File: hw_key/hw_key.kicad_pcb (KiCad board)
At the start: 2 copper layers, 127 x 38.1 mm, 27 parts, among them P2 CONN_01X10, SW1 SW_PUSH_SMALL_H, SW10 SW_PUSH_SMALL_H, SW11 SW_PUSH_SMALL_H, SW12 SW_PUSH_SMALL_H, SW2 SW_PUSH_SMALL_H, SW3 SW_PUSH_SMALL_H, SW4 SW_PUSH_SMALL_H, SW5 SW_PUSH_SMALL_H, SW6 SW_PUSH_SMALL_H, SW7 SW_PUSH_SMALL_H, SW8 SW_PUSH_SMALL_H, SW9 SW_PUSH_SMALL_H

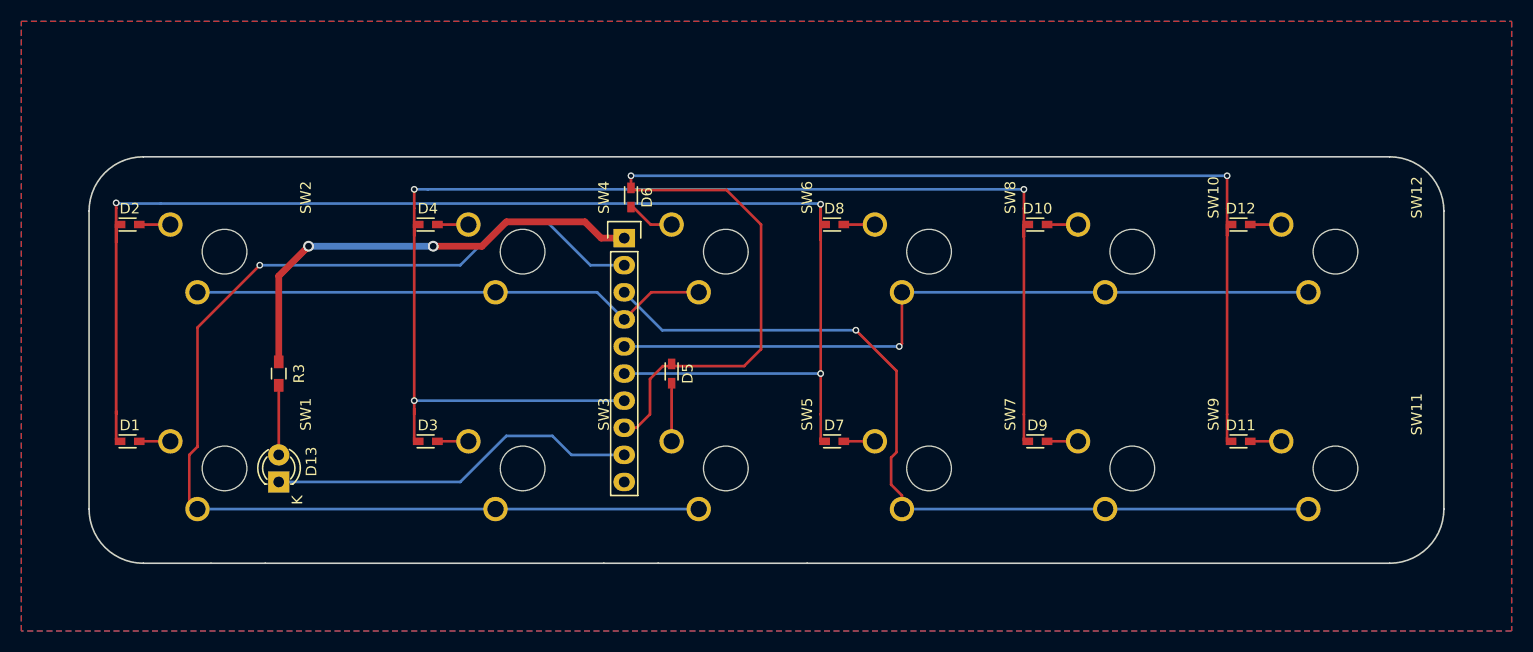
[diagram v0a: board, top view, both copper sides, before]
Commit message: misc, rst button 3d model
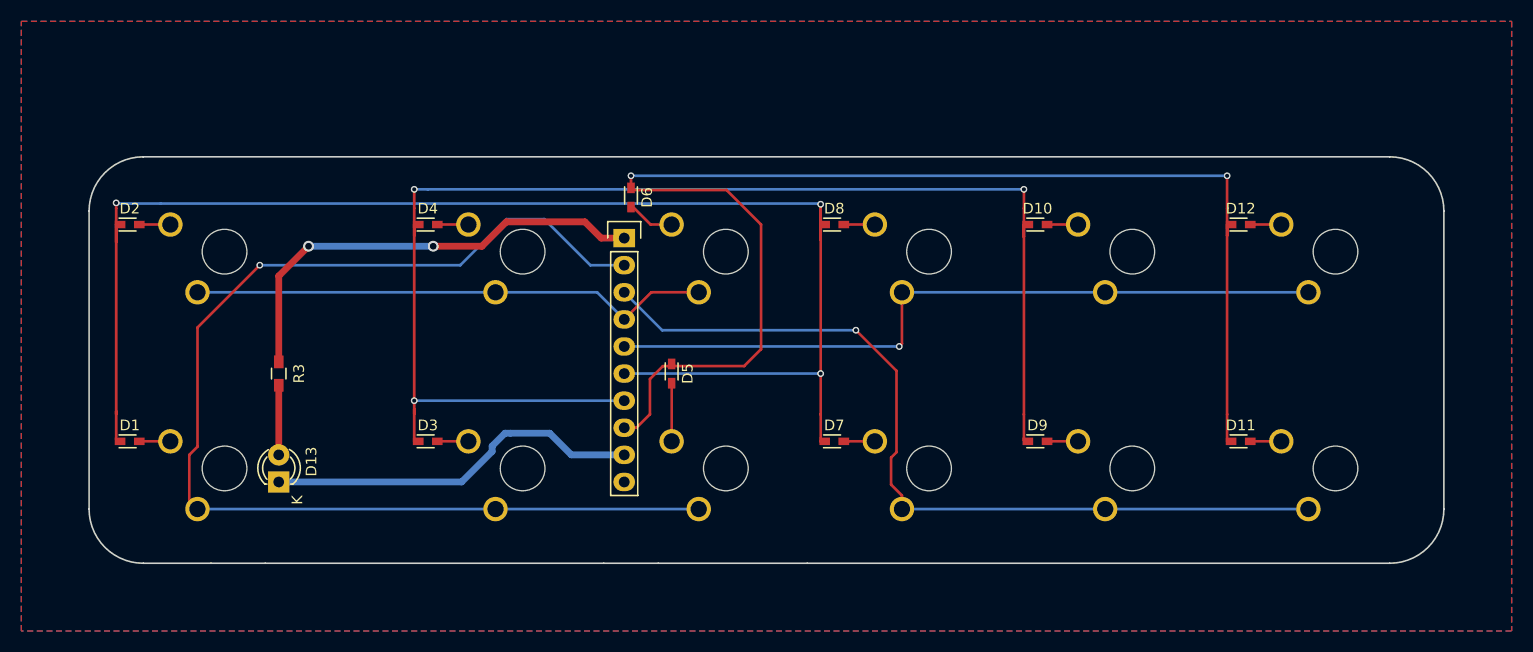
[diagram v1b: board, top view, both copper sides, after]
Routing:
- net /kLED_MACRO: track 34.9 -> 35.4 mm
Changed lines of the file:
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@@
     (thickness 1.6)
     (drawings 14)
-    (tracks 137)
+    (tracks 140)
     (zones 0)
     (modules 27)
@@
     (visible_elements 7FFEFFFF)
     (pcbplotparams
-      (layerselection 0x00030_80000001)
-      (usegerberextensions false)
+      (layerselection 0x010fc_80000001)
+      (usegerberextensions true)
       (excludeedgelayer true)
       (linewidth 0.100000)
       (plotframeref false)
-      (viasonmask false)
+      (viasonmask true)
       (mode 1)
-      (useauxorigin false)
+      (useauxorigin true)
       (hpglpennumber 1)
       (hpglpenspeed 20)
@@
       (psa4output false)
       (plotreference true)
-      (plotvalue true)
+      (plotvalue false)
       (plotinvisibletext false)
       (padsonsilk false)
-      (subtractmaskfromsilk false)
+      (subtractmaskfromsilk true)
       (outputformat 1)
       (mirror false)
-      (drillshape 1)
+      (drillshape 0)
       (scaleselection 1)
-      (outputdirectory ""))
+      (outputdirectory grb))
   )
   (net 0 "")
@@
     (add_net /kC2)
     (add_net /kC3)
-    (add_net /kLED_MACRO)
     (add_net /kR0)
     (add_net /kR1)
@@
     (add_net "Net-(D11-Pad2)")
     (add_net "Net-(D12-Pad2)")
-    (add_net "Net-(D13-Pad2)")
     (add_net "Net-(D2-Pad2)")
     (add_net "Net-(D3-Pad2)")
@@
     (uvia_drill 0.1016)
     (add_net +3V3)
+    (add_net /kLED_MACRO)
     (add_net GND)
+    (add_net "Net-(D13-Pad2)")
   )
   (module Pin_Headers:Pin_Header_Straight_1x10 (layer F.Cu)
@@
   (module components:CHERRY_MX (layer F.Cu)
     (at 38.1 54.61 90)
-    (fp_text reference SW1 (at 5.08 7.62 90) (layer F.SilkS)
+    (fp_text reference SW1 (at 5.08 7.62 90) (layer F.SilkS) hide
       (effects (font (size 1 1) (thickness 0.15)))
     )
@@
   (module components:CHERRY_MX (layer F.Cu)
     (at 38.1 34.29 90)
-    (fp_text reference SW2 (at 5.08 7.62 90) (layer F.SilkS)
+    (fp_text reference SW2 (at 5.08 7.62 90) (layer F.SilkS) hide
       (effects (font (size 1 1) (thickness 0.15)))
     )
@@
   (module components:CHERRY_MX (layer F.Cu)
     (at 66.04 54.61 90)
-    (fp_text reference SW3 (at 5.08 7.62 90) (layer F.SilkS)
+    (fp_text reference SW3 (at 5.08 7.62 90) (layer F.SilkS) hide
       (effects (font (size 1 1) (thickness 0.15)))
     )
@@
   (module components:CHERRY_MX (layer F.Cu)
     (at 66.04 34.29 90)
-    (fp_text reference SW4 (at 5.08 7.62 90) (layer F.SilkS)
+    (fp_text reference SW4 (at 5.08 7.62 90) (layer F.SilkS) hide
       (effects (font (size 1 1) (thickness 0.15)))
     )
@@
   (module components:CHERRY_MX (layer F.Cu)
     (at 85.09 54.61 90)
-    (fp_text reference SW5 (at 5.08 7.62 90) (layer F.SilkS)
+    (fp_text reference SW5 (at 5.08 7.62 90) (layer F.SilkS) hide
       (effects (font (size 1 1) (thickness 0.15)))
     )
@@
   (module components:CHERRY_MX (layer F.Cu)
     (at 85.09 34.29 90)
-    (fp_text reference SW6 (at 5.08 7.62 90) (layer F.SilkS)
+    (fp_text reference SW6 (at 5.08 7.62 90) (layer F.SilkS) hide
       (effects (font (size 1 1) (thickness 0.15)))
     )
@@
   (module components:CHERRY_MX (layer F.Cu)
     (at 104.14 54.61 90)
-    (fp_text reference SW7 (at 5.08 7.62 90) (layer F.SilkS)
+    (fp_text reference SW7 (at 5.08 7.62 90) (layer F.SilkS) hide
       (effects (font (size 1 1) (thickness 0.15)))
     )
@@
   (module components:CHERRY_MX (layer F.Cu)
     (at 104.14 34.29 90)
-    (fp_text reference SW8 (at 5.08 7.62 90) (layer F.SilkS)
+    (fp_text reference SW8 (at 5.08 7.62 90) (layer F.SilkS) hide
       (effects (font (size 1 1) (thickness 0.15)))
     )
@@
   (module components:CHERRY_MX (layer F.Cu)
     (at 123.19 54.61 90)
-    (fp_text reference SW9 (at 5.08 7.62 90) (layer F.SilkS)
+    (fp_text reference SW9 (at 5.08 7.62 90) (layer F.SilkS) hide
       (effects (font (size 1 1) (thickness 0.15)))
     )
@@
   (module components:CHERRY_MX (layer F.Cu)
     (at 123.19 34.29 90)
-    (fp_text reference SW10 (at 5.08 7.62 90) (layer F.SilkS)
+    (fp_text reference SW10 (at 5.08 7.62 90) (layer F.SilkS) hide
       (effects (font (size 1 1) (thickness 0.15)))
     )
@@
   (module components:CHERRY_MX (layer F.Cu)
     (at 142.24 54.61 90)
-    (fp_text reference SW11 (at 5.08 7.62 90) (layer F.SilkS)
+    (fp_text reference SW11 (at 5.08 7.62 90) (layer F.SilkS) hide
       (effects (font (size 1 1) (thickness 0.15)))
     )
@@
   (module components:CHERRY_MX (layer F.Cu)
     (at 142.24 34.29 90)
-    (fp_text reference SW12 (at 5.08 7.62 90) (layer F.SilkS)
+    (fp_text reference SW12 (at 5.08 7.62 90) (layer F.SilkS) hide
       (effects (font (size 1 1) (thickness 0.15)))
     )
@@
   (segment (start 137.16 52.07) (end 134.25 52.07) (width 0.254) (layer F.Cu) (net 11))
   (segment (start 137.16 31.75) (end 134.25 31.75) (width 0.254) (layer F.Cu) (net 12))
-  (segment (start 43.18 53.34) (end 43.18 46.82) (width 0.254) (layer F.Cu) (net 13) (status 30))
+  (segment (start 43.18 53.34) (end 43.18 46.82) (width 0.635) (layer F.Cu) (net 13) (status 30))
   (segment (start 43.18 44.62) (end 43.18 36.576) (width 0.635) (layer F.Cu) (net 14) (status 10))
   (segment (start 73.406 33.02) (end 75.565 33.02) (width 0.635) (layer F.Cu) (net 14) (status 20))
@@
   (segment (start 88.392 43.434) (end 88.392 31.75) (width 0.254) (layer F.Cu) (net 17))
   (segment (start 86.806 45.02) (end 88.392 43.434) (width 0.254) (layer F.Cu) (net 17))
-  (segment (start 75.565 53.34) (end 70.612 53.34) (width 0.254) (layer B.Cu) (net 18))
-  (segment (start 60.198 55.88) (end 43.18 55.88) (width 0.254) (layer B.Cu) (net 18))
-  (segment (start 64.516 51.562) (end 60.198 55.88) (width 0.254) (layer B.Cu) (net 18))
-  (segment (start 68.834 51.562) (end 64.516 51.562) (width 0.254) (layer B.Cu) (net 18))
-  (segment (start 70.612 53.34) (end 68.834 51.562) (width 0.254) (layer B.Cu) (net 18))
+  (segment (start 64.897 51.308) (end 64.389 51.308) (width 0.635) (layer B.Cu) (net 18))
+  (segment (start 70.612 53.34) (end 68.58 51.308) (width 0.635) (layer B.Cu) (net 18))
+  (segment (start 68.58 51.308) (end 64.897 51.308) (width 0.635) (layer B.Cu) (net 18))
+  (segment (start 43.18 55.88) (end 60.325 55.88) (width 0.635) (layer B.Cu) (net 18) (status 400000))
+  (segment (start 70.612 53.34) (end 75.565 53.34) (width 0.635) (layer B.Cu) (net 18))
+  (segment (start 63.1825 53.0225) (end 60.325 55.88) (width 0.635) (layer B.Cu) (net 18))
+  (segment (start 63.1825 52.5145) (end 63.1825 53.0225) (width 0.635) (layer B.Cu) (net 18))
+  (segment (start 64.389 51.308) (end 63.1825 52.5145) (width 0.635) (layer B.Cu) (net 18))
   (segment (start 75.565 43.18) (end 101.346 43.18) (width 0.254) (layer B.Cu) (net 19) (status 10))
   (segment (start 101.6 42.926) (end 101.6 38.1) (width 0.254) (layer F.Cu) (net 19) (status 20))
@@
   (segment (start 34.798 57.658) (end 34.798 53.34) (width 0.254) (layer F.Cu) (net 21) (status 10))
   (segment (start 72.39 35.56) (end 75.565 35.56) (width 0.254) (layer B.Cu) (net 21) (status 20))
-  (segment (start 68.326 31.496) (end 72.39 35.56) (width 0.254) (layer B.Cu) (net 21))
-  (segment (start 64.262 31.496) (end 68.326 31.496) (width 0.254) (layer B.Cu) (net 21))
-  (segment (start 60.198 35.56) (end 64.262 31.496) (width 0.254) (layer B.Cu) (net 21))
+  (segment (start 68.072 31.242) (end 72.39 35.56) (width 0.254) (layer B.Cu) (net 21))
+  (segment (start 64.516 31.242) (end 68.072 31.242) (width 0.254) (layer B.Cu) (net 21))
+  (segment (start 60.198 35.56) (end 64.516 31.242) (width 0.254) (layer B.Cu) (net 21))
   (segment (start 41.402 35.56) (end 60.198 35.56) (width 0.254) (layer B.Cu) (net 21))
   (via (at 41.402 35.56) (size 0.635) (drill 0.381) (layers F.Cu B.Cu) (net 21))

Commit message: mounting holes
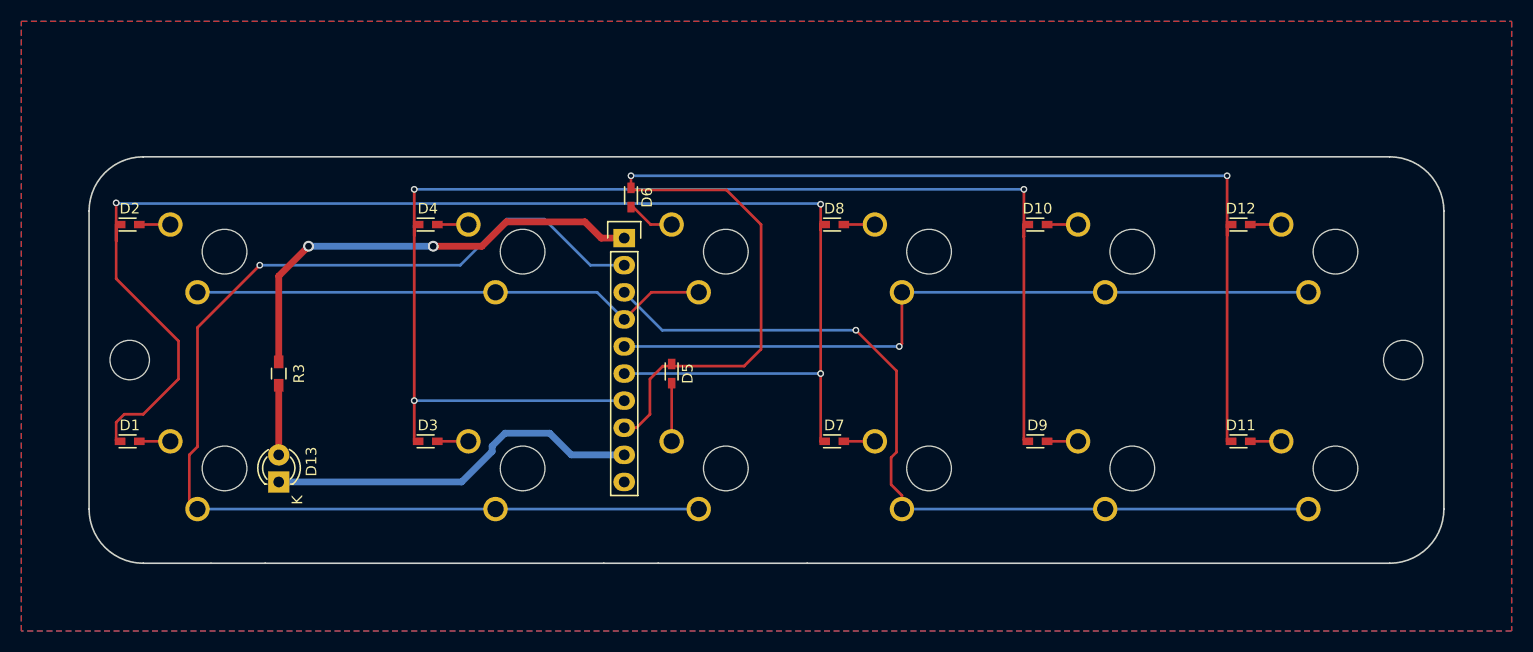
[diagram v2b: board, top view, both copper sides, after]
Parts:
- added REF**: MountingHole_3.7mm, Mounting_Holes:MountingHole_3.7mm, F.Cu at (148.6, 44.5)
- added REF**: MountingHole_3.7mm, Mounting_Holes:MountingHole_3.7mm, F.Cu at (29.2, 44.5)
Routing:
- net /kR0: track 136.0 -> 139.1 mm
- net /kR1: track 128.2 -> 127.6 mm

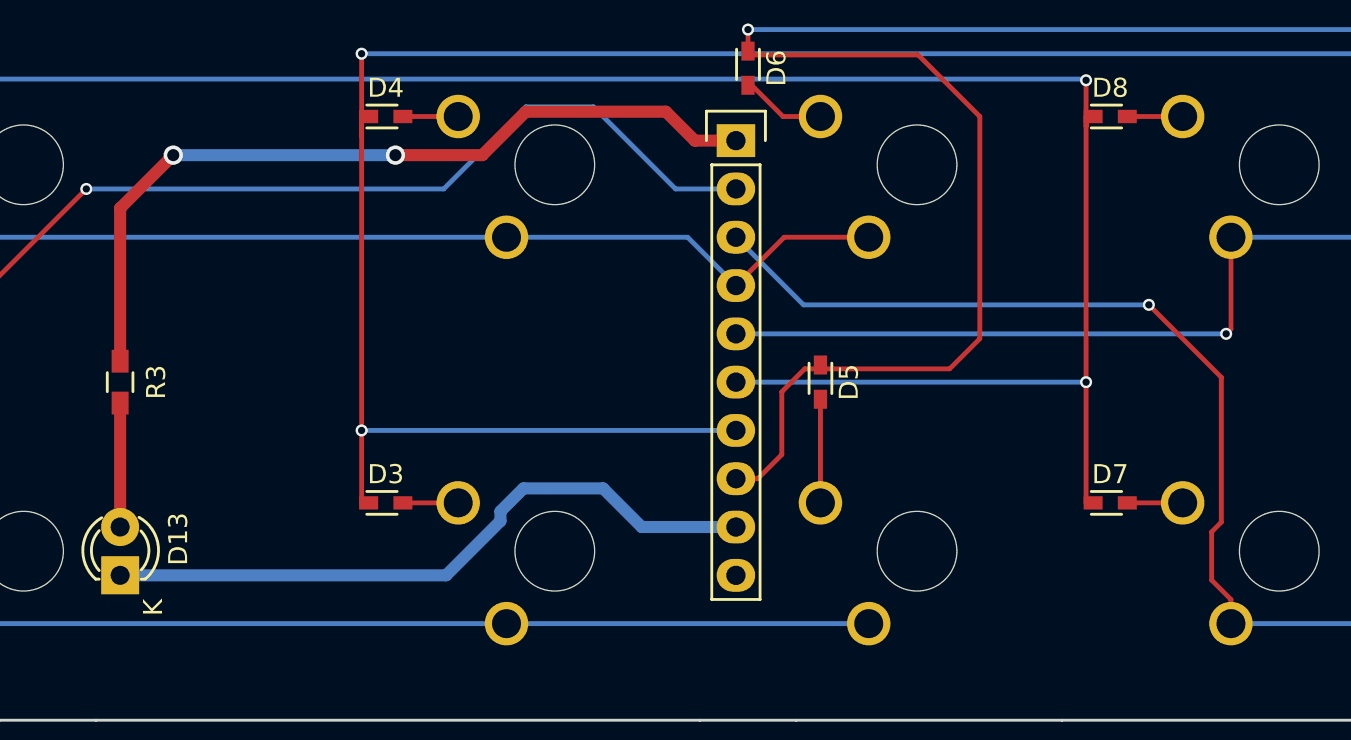
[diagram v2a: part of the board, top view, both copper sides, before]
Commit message: correct pin layouts
as per breadboard test
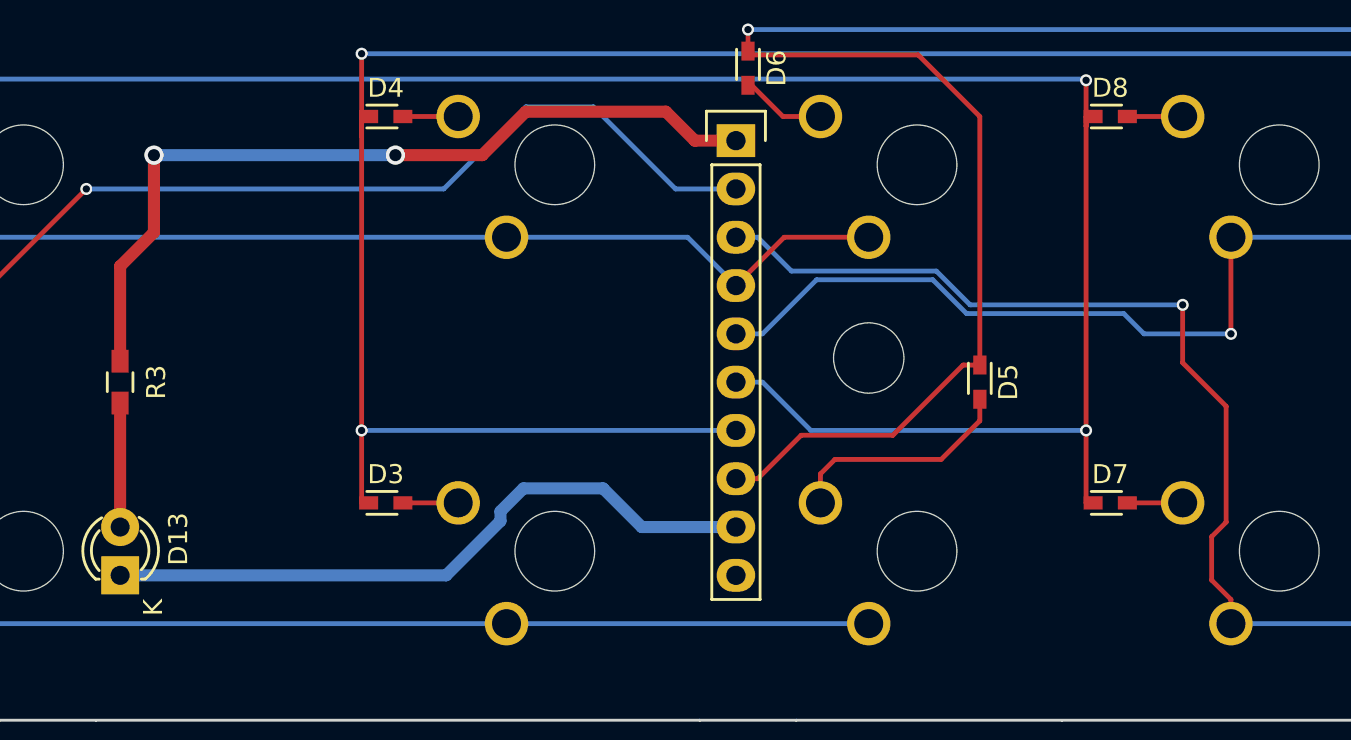
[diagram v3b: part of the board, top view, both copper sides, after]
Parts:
- added REF**: MountingHole_3.7mm, Mounting_Holes:MountingHole_3.7mm, F.Cu at (82.5, 44.5)
- moved D5 8.38 mm to (88.4, 45.7)
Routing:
- net Net-(D5-Pad2): track 5.65 -> 12.2 mm
- net /kC3: track 69.1 -> 71.6 mm
- net /kC1: track 80.3 -> 81.5 mm
- net /kR2: track 126.9 -> 125.8 mm
- net /kR0: track 139.1 -> 140.1 mm
- net +3V3: track 43.2 -> 43.8 mm
